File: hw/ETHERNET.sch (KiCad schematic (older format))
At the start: 29 parts, among them J2 RB1-125B8G1A, U5 RTL8211EG-VB-CG, X1 SG-7050CAN

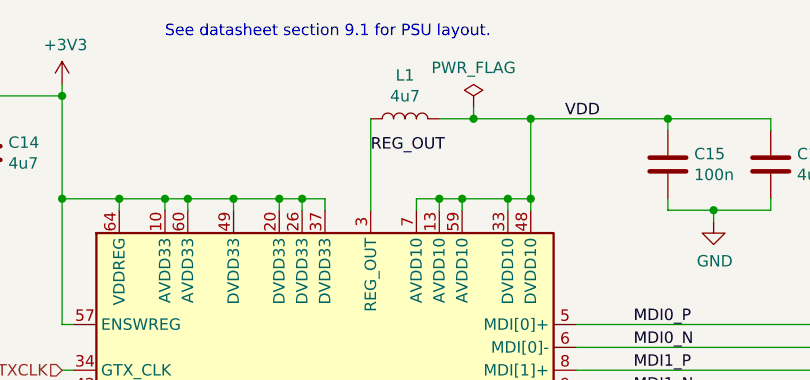
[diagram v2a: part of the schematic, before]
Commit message: Replace ethernet SMPS inductor with a sensible power rating
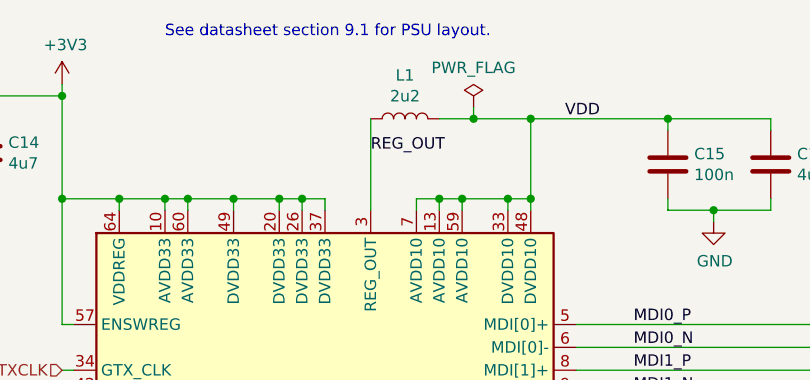
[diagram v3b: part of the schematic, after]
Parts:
- L1: value 4u7 -> 2u2; footprint Resistor_SMD:R_0603_1608Metric -> Inductor_SMD:L_Sunlord_MWSA0518; LCSC Part C19666 -> C408345
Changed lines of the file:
@@
 P 6450 1250
 F 0 "L1" V 6640 1250 50  0000 C CNN
-F 1 "4u7" V 6549 1250 50  0000 C CNN
-F 2 "Resistor_SMD:R_0603_1608Metric" H 6450 1250 50  0001 C CNN
+F 1 "2u2" V 6549 1250 50  0000 C CNN
+F 2 "Inductor_SMD:L_Sunlord_MWSA0518" H 6450 1250 50  0001 C CNN
 F 3 "~" H 6450 1250 50  0001 C CNN
-F 4 "C19666" H 6640 1350 50  0001 C CNN "LCSC Part"
+F 4 "C408345" H 6640 1350 50  0001 C CNN "LCSC Part"
 	1    6450 1250
 	0    -1   -1   0

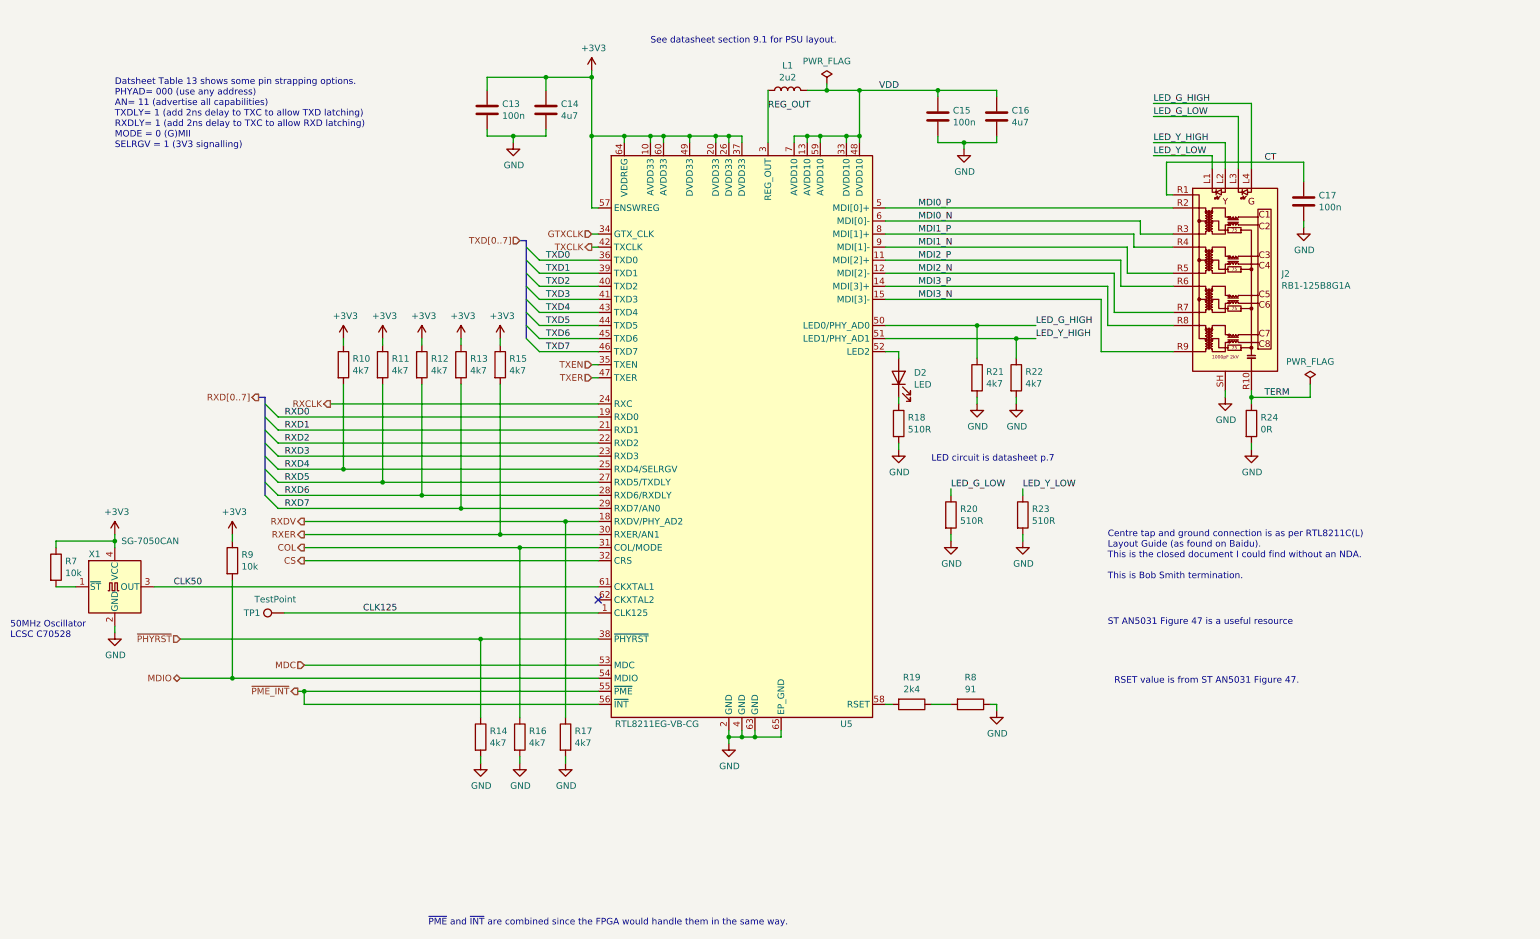
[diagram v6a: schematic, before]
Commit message: Add ESD protection
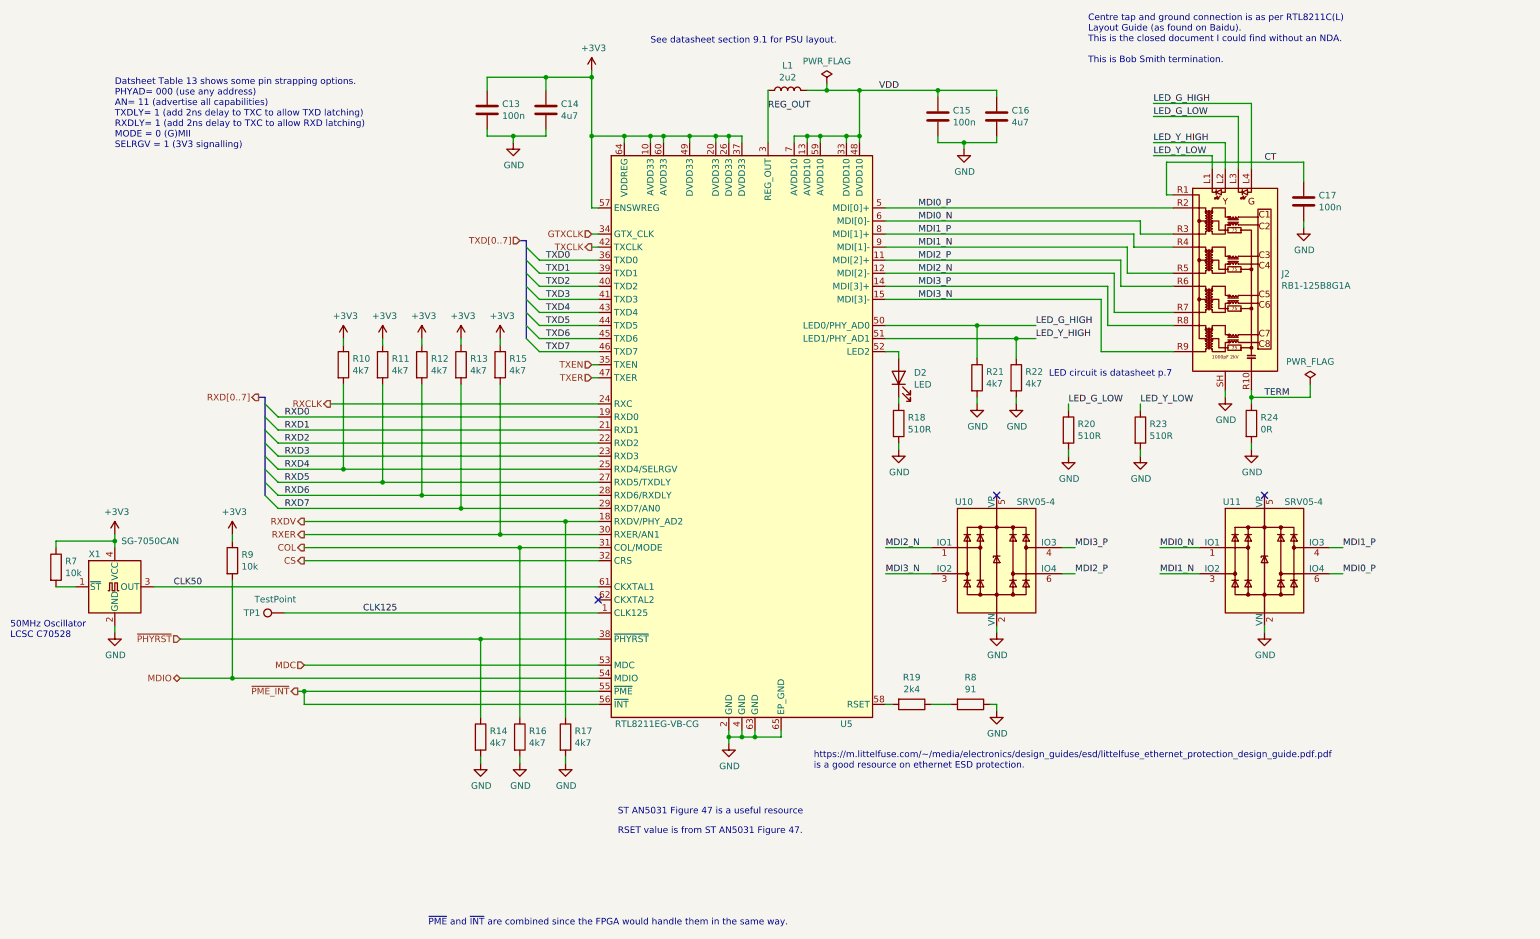
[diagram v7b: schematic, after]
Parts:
- added U10, U11: SRV05-4, Package_TO_SOT_SMD:SOT-23-6, symbol Power_Protection:SRV05-4
- L1: footprint Inductor_SMD:L_Sunlord_MWSA0518 -> Inductor_SMD:L_Sunlord_MWSA0518_5.4x5.2mm
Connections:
- net GND: now also U10.2 (VN), U11.2 (VN)
- net MDI0_N: now also U11.1 (IO1)
- net MDI0_P: now also U11.6 (IO4)
- net MDI1_N: now also U11.3 (IO2)
- net MDI1_P: now also U11.4 (IO3)
- net MDI2_N: now also U10.1 (IO1)
- net MDI2_P: now also U10.6 (IO4)
- net MDI3_N: now also U10.3 (IO2)
- net MDI3_P: now also U10.4 (IO3)
- no-connect marks 1 -> 3
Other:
- note added: "https://m.littelfuse.com/~~/media/electronics/design_guides/esd/littelfuse_ethernet_protection_design_guide.pdf.pdf\nis a good resource on ethernet ESD protection."
- moved on the sheet: R20, R23

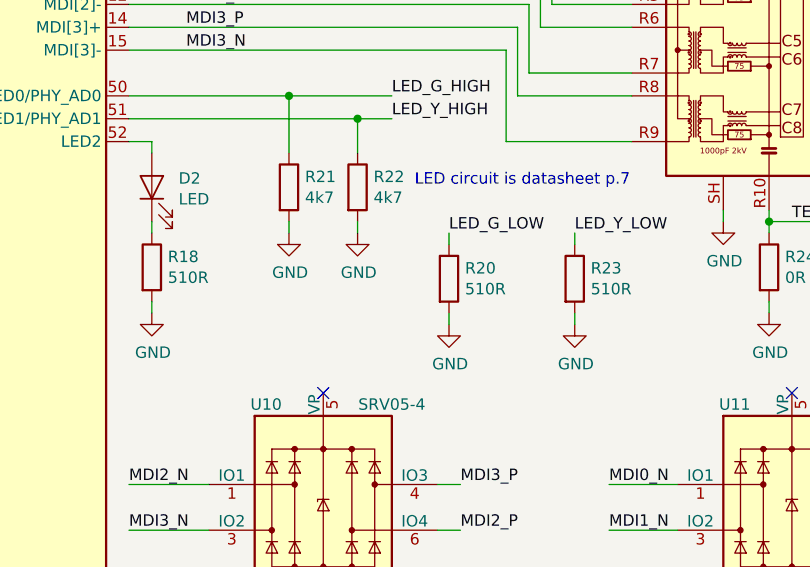
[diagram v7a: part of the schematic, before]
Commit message: Fix JLC rotation
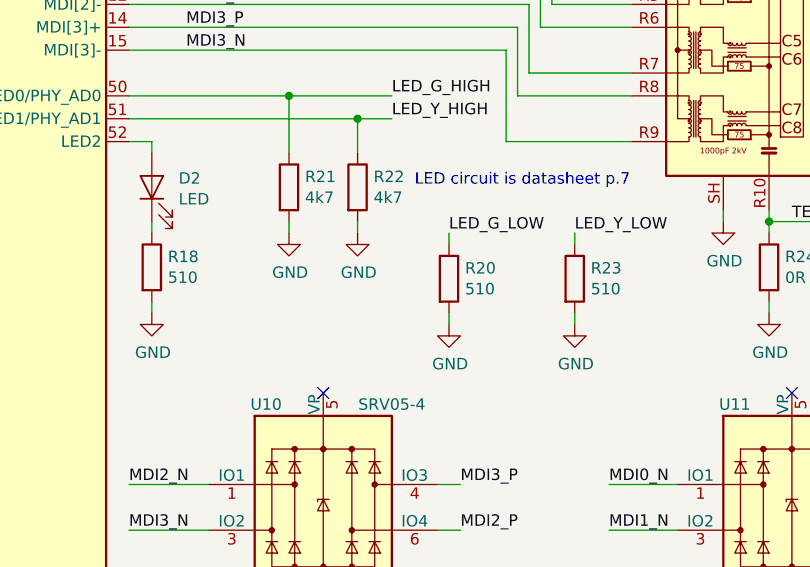
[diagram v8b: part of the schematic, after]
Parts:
- C13, C14, C15, C16, C17, D2, L1, R10, R11, R12, R13, R14, R15, R16, R17, R19, R21, R22, R24, R7, R8, R9, U5, X1: JLCPCB Rotation (none) -> 0
- R18, R20, R23: value 510R -> 510; JLCPCB Rotation (none) -> 0
- U10, U11: JLCPCB Rotation (none) -> 180
